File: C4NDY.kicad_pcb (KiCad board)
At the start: 2 copper layers, 22.9 x 50.2 mm, 42 parts, among them J1 Conn_01x08, J2 Conn_01x07, J3 Conn_01x05, J4 5077CR-16SMC2-BK-TR, J5 Conn_01x06, J6 Conn_01x08, J7 FTSH-105-01-L-DV-K, SW1 SKRPABE010, SW2 SKRPABE010, U1 MIC39100-3.3WS, U2 IS66WVS2M8BLL, U3 CETx, X1 SG-310SCF

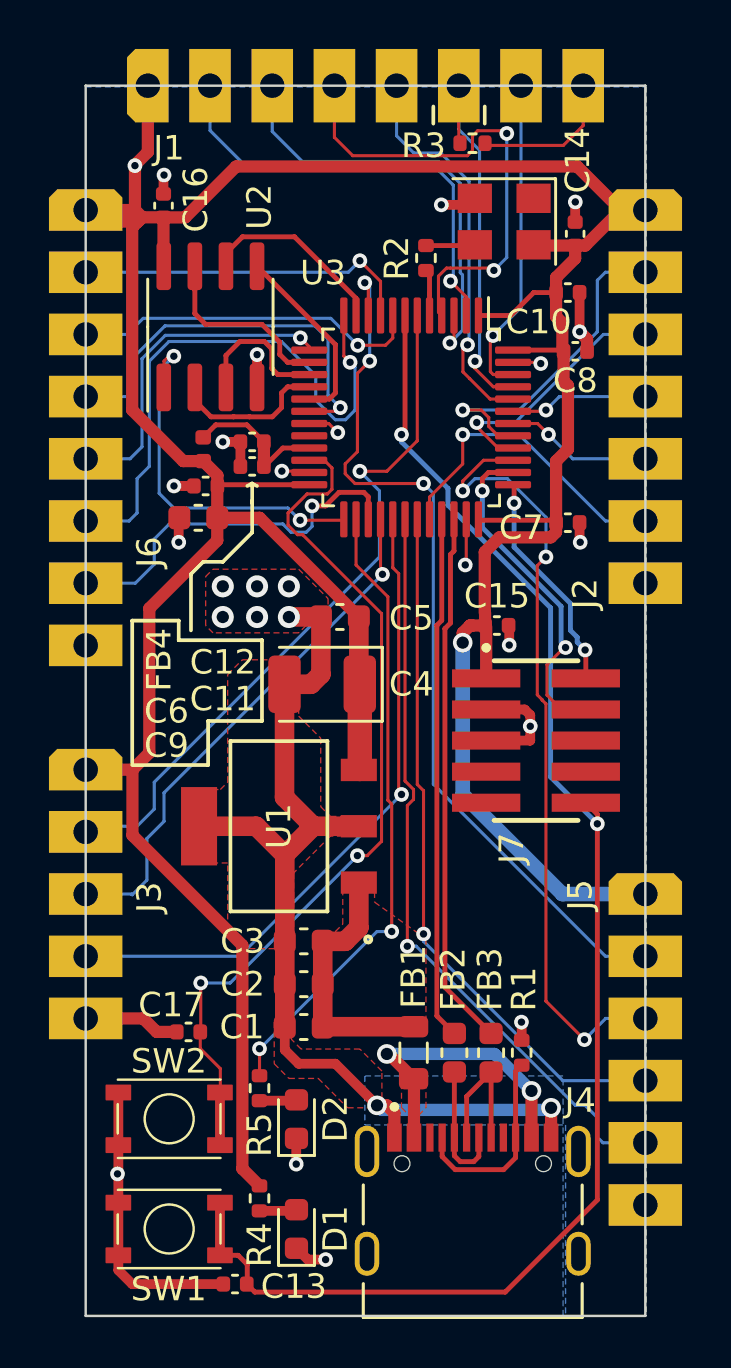
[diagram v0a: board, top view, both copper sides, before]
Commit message: Fix some mistakes.
1．A1_XXをA12_XXに修正
2．ビアに被っていたシルクの位置を調整
3．USB Type-CのCC用5.1kをまとめない
4．スイッチのフットプリントを修正
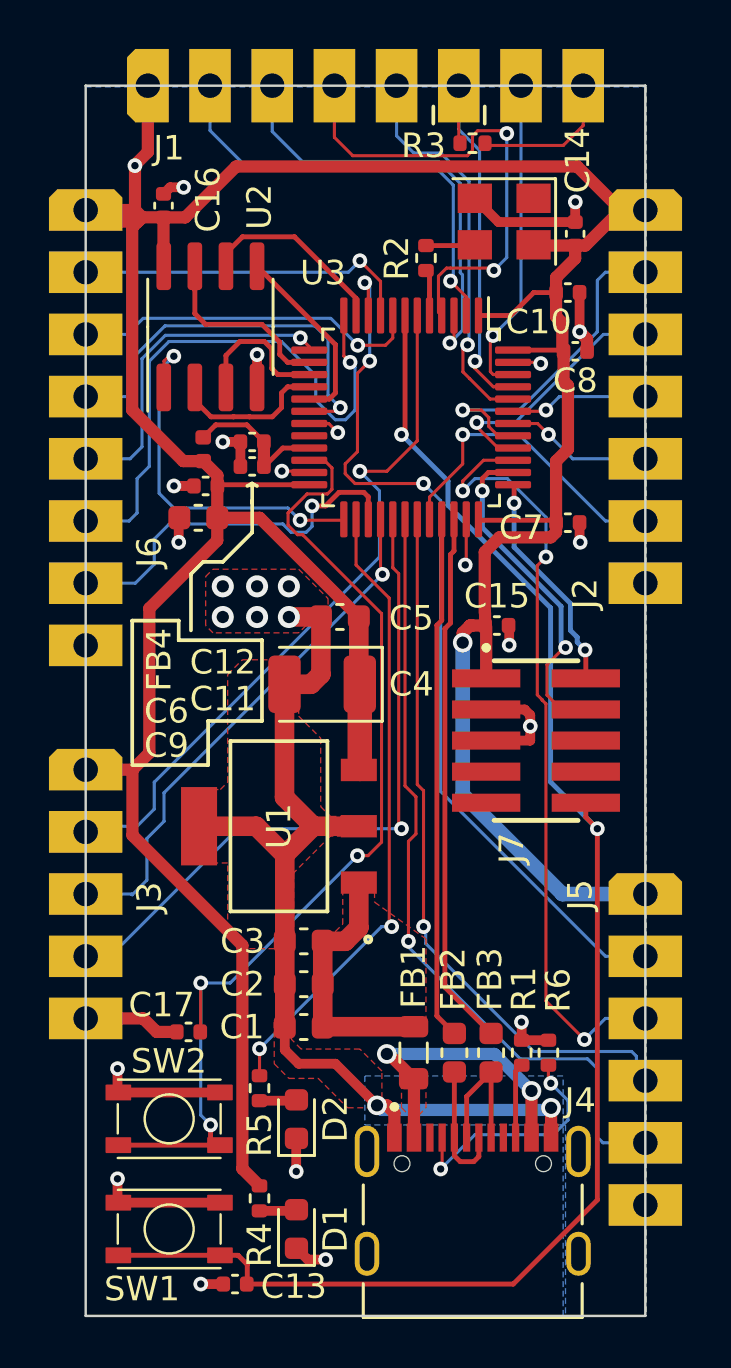
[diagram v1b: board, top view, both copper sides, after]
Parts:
- added R6: 5.1k, Resistor_SMD:R_0402_1005Metric, F.Cu at (148.9, 119.2)
- R2: value 10 -> 33
- U3: value CETx -> STM32G4A1CETx
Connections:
- J4 pad A5: /CC -> Net-(J4-CC1)
- J4 pad B5: /CC -> Net-(J4-CC2)
- R1 pad 1: /CC -> Net-(J4-CC2)
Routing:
- net Net-(J4-CC1): track 0.00 -> 9.91 mm, vias 0 -> 2
- net /CC: track 8.08 -> 0.00 mm
- net Net-(SW2-A): track 36.0 -> 42.0 mm, vias 2 -> 3
- net GND: track 89.5 -> 93.5 mm, vias 27 -> 28
- net Net-(J4-CC2): track 0.00 -> 3.06 mm
- net /NRST: track 61.4 -> 63.3 mm
- net /I2C_SDA: track 31.2 -> 32.4 mm
- net /SPI_MOSI: track 26.0 -> 26.8 mm
- net /I2C_SCL: track 28.4 -> 29.0 mm
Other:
- board text added: "rev.B"
- board text removed: "rev.A"

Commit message: Fixed some comment.
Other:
- board text added: "UNIT:mm PAD SIZE:3 x 1.7 PITCH:2.54"
- board text added: "[OTHER] 28:PB9 29:PB8/BOOT0(10k pull-down) 30:PB7 31:PC15 32:PC14 33:C13 [ONBOARD] LED:PB12 SW:PB10 QSPI_NCS:PB11 QSPI_CLK:PA3 QSPI_IO0:PB1 QSPI_IO1:PB0 QSPI_IO2:PA7 QSPI_IO3:PA6"
- board text removed: "UNIT:mm PAD SIZE:3mm x 1.7mm PITCH:2.54mm"
- board text removed: "[OTHER] 28:PB9 29:PB8/BOOT0(10k pull-down) 30:PB7 31:PC15 32:PC14 33:C13"
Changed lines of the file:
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@@
     (effects (font (size 1 1) (thickness 0.1875)) (justify left bottom mirror))
   )
-  (gr_text "[OTHER]\n28:PB9\n29:PB8/BOOT0(10k pull-down)\n30:PB7\n31:PC15\n32:PC14\n33:C13" (at 185.8 91.8) (layer "Cmts.User")
+  (gr_text "[OTHER]\n28:PB9\n29:PB8/BOOT0(10k pull-down)\n30:PB7\n31:PC15\n32:PC14\n33:C13\n\n[ONBOARD]\nLED:PB12\nSW:PB10\nQSPI_NCS:PB11\nQSPI_CLK:PA3\nQSPI_IO0:PB1\nQSPI_IO1:PB0\nQSPI_IO2:PA7\nQSPI_IO3:PA6" (at 186 107.7) (layer "Cmts.User")
     (effects (font (size 1 1) (thickness 0.15)) (justify left bottom))
   )
-  (gr_text "UNIT:mm\nPAD SIZE:3mm x 1.7mm\nPITCH:2.54mm" (at 158.6 75.87) (layer "Cmts.User")
+  (gr_text "UNIT:mm\nPAD SIZE:3 x 1.7\nPITCH:2.54" (at 158.6 75.87) (layer "Cmts.User")
     (effects (font (size 1 1) (thickness 0.15)) (justify left bottom))
   )
